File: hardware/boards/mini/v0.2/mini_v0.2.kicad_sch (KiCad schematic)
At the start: 99 parts, among them IC1 NAU88C22YG, IC3 IS42S16160J-6BLI, J2 Top, J3 Bottom, Q1 PMV37EN22, U1 W25Q128JVP, U2 LTV-217-G, U4 STM32H750XBHx, Y1 Crystal_GND24, Y3 32.768kHz

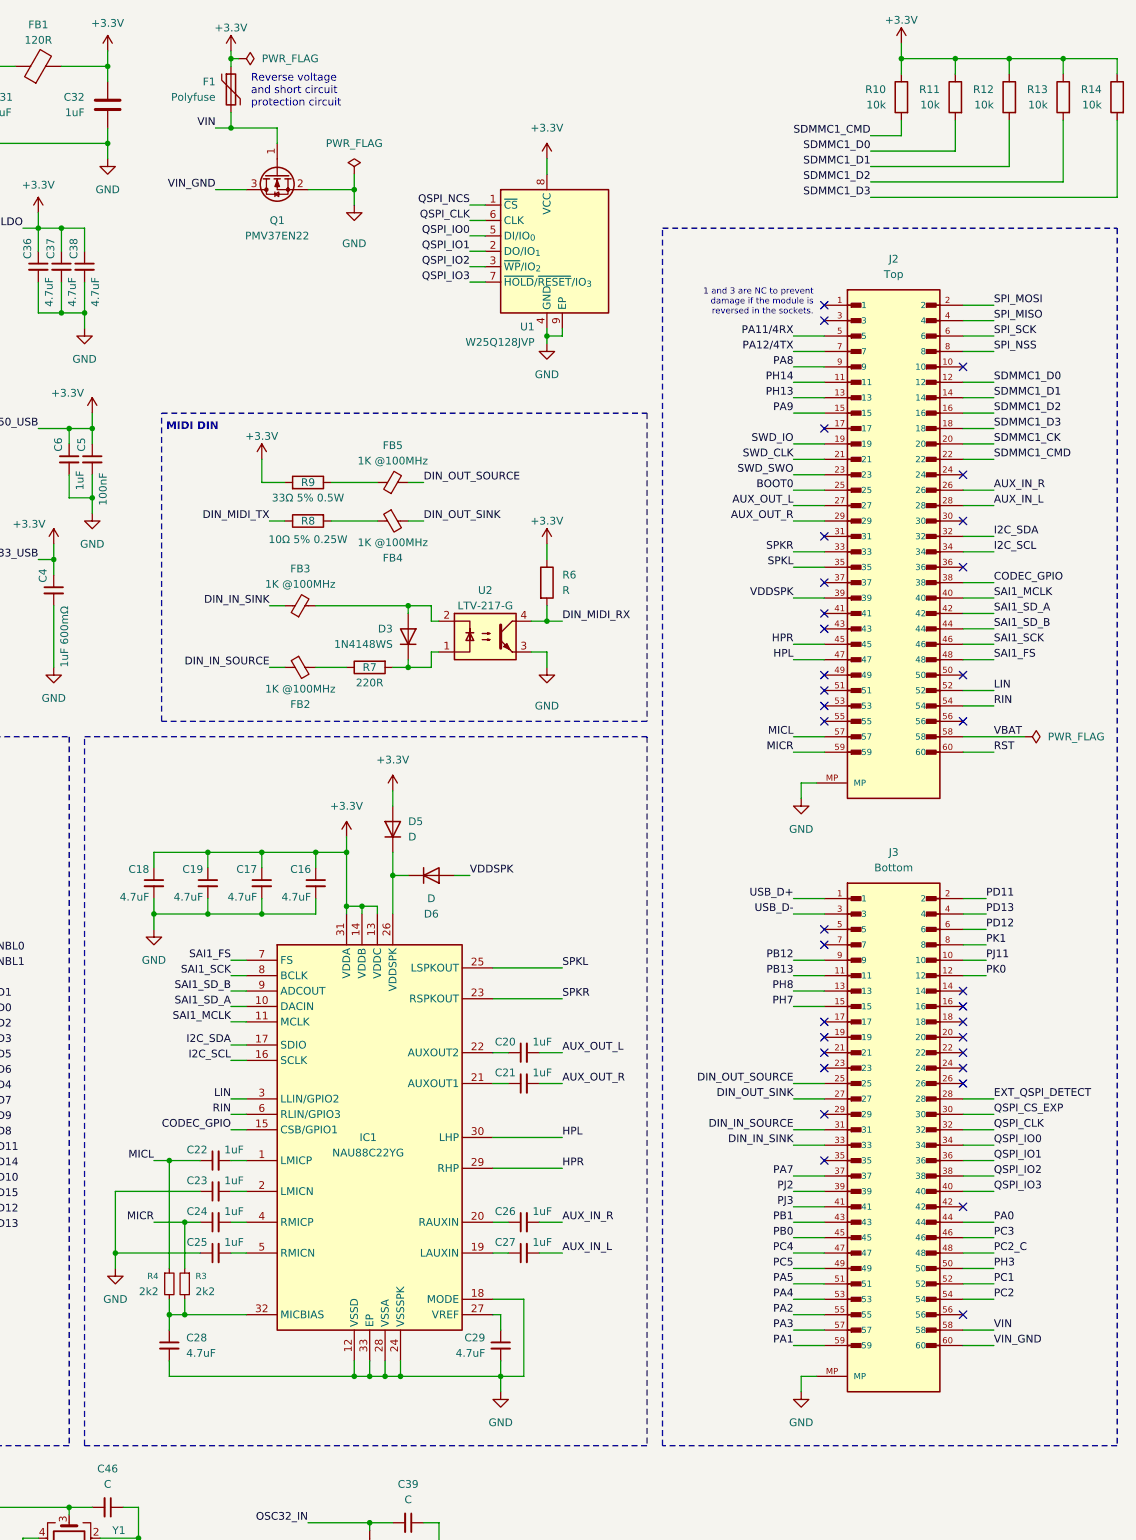
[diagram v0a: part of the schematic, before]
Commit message: mini: start adding symbol for mating footprint
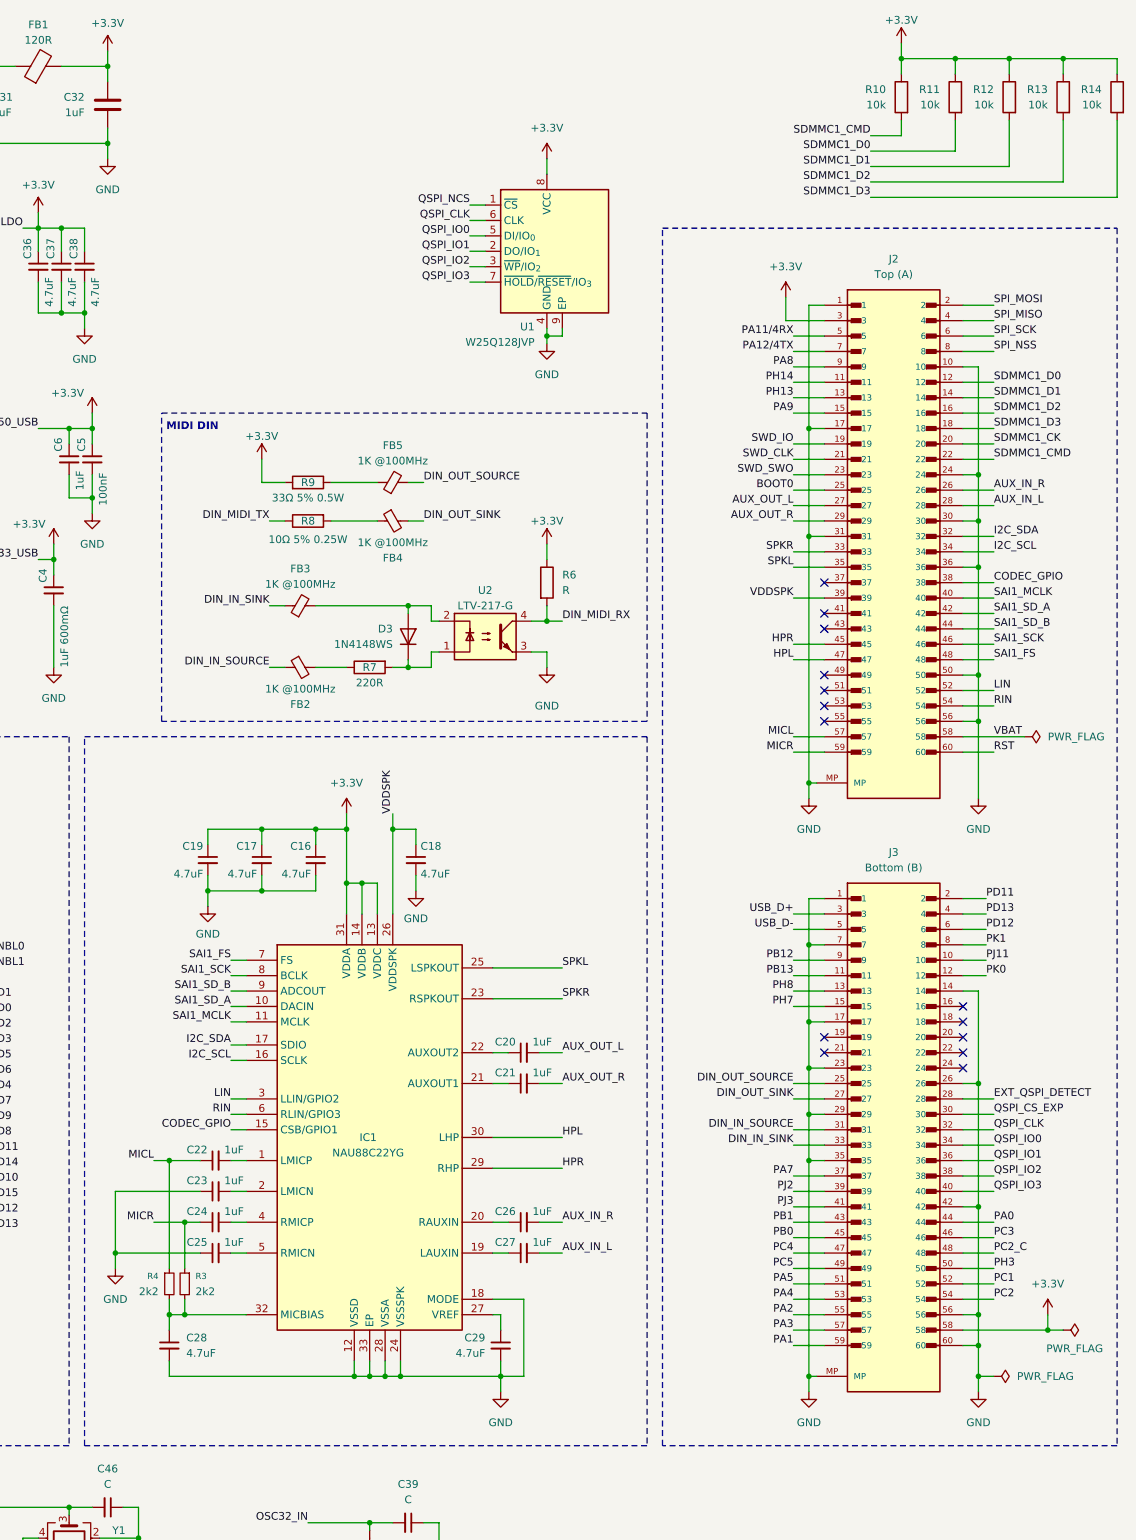
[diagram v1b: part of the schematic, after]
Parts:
- removed D5, D6: D, Diode_SMD:D_0402_1005Metric, symbol Device:D
- removed F1: Polyfuse, Fuse:Fuse_0805_2012Metric, symbol Device:Polyfuse
- removed Q1: PMV37EN22, Package_TO_SOT_SMD:TSOT-23, symbol Transistor_FET:Q_NMOS_GSD
- J2: value Top -> Top (A)
- J3: value Bottom -> Bottom (B)
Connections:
- net VIN is gone; now on net +3.3V: J3.58
- net VIN_GND is gone; now on net GND: J3.60
- net +3.3V: now also J2.3; no longer C18.1
- net GND: now also J2.1, J2.10, J2.17, J2.24, J2.30, J2.31, J2.36, J2.50, J2.56, J3.1, J3.14, J3.17, J3.23, J3.26, J3.29, J3.35, J3.42, J3.56, J3.7
- net USB_D+: now also J3.3; no longer J3.1
- net USB_D-: now also J3.5; no longer J3.3
- net VDDSPK: now also C18.1, IC1.26 (VDDSPK)
- no-connect marks 95 -> 75
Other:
- note removed: "1 and 3 are NC to prevent damage if the module is reversed in the sockets."
- note removed: "Reverse voltage and short circuit protection circuit"
- moved on the sheet: C16, C17, C18, C19
